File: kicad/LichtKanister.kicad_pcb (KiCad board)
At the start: 2 copper layers, 38 x 38 mm, 21 parts, among them J1 AVR-ISP-6, J2 Conn_01x04, J3 Conn_01x03, U1 ATmega48-20AU, U2 MAX485E, Y1 Crystal

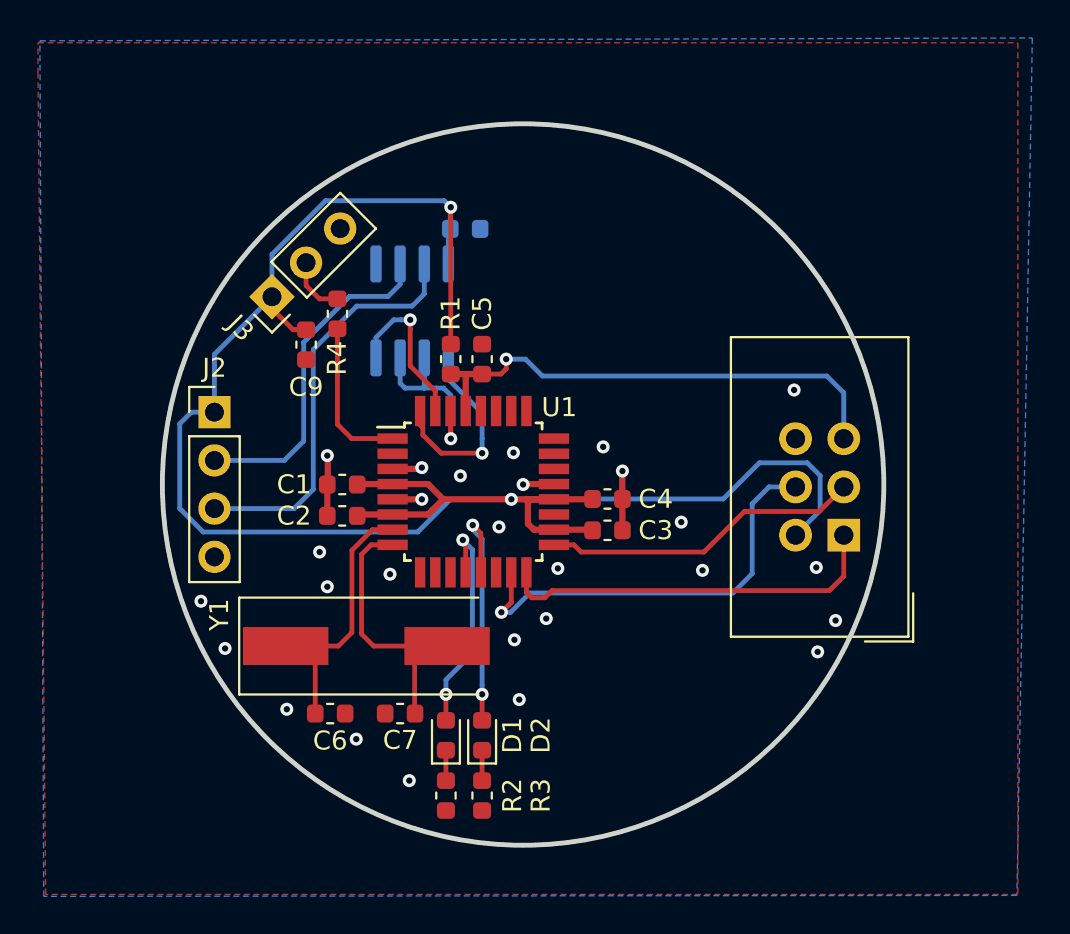
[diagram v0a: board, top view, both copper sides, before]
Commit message: added Mounting Holes, PinHeader for addressing first iteration of routing done
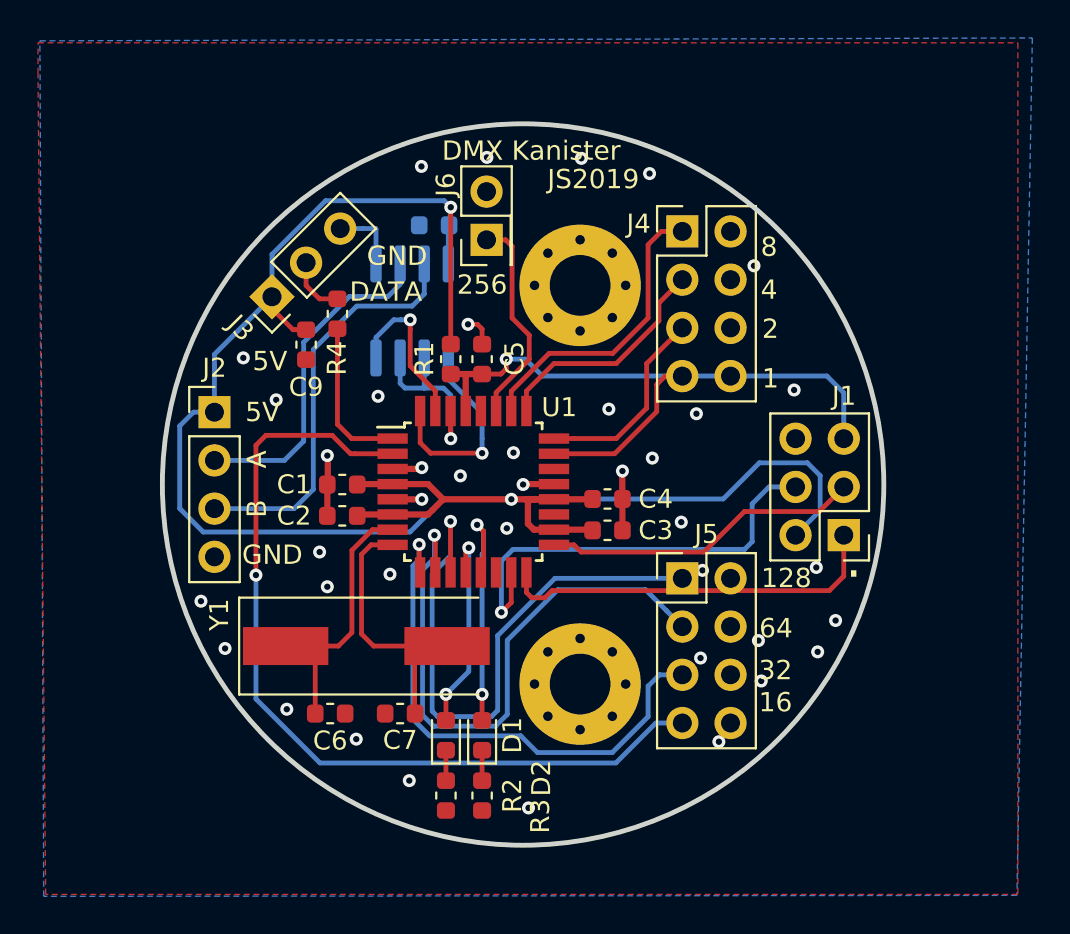
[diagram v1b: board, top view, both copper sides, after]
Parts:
- added H1: MountingHole_Pad, MountingHole:MountingHole_3.2mm_M3_Pad_Via, F.Cu at (73.5, 80.7)
- added H2: MountingHole_Pad, MountingHole:MountingHole_3.2mm_M3_Pad_Via, F.Cu at (73.5, 101.7)
- added J4: Conn_02x04_Odd_Even, Connector_PinHeader_2.54mm:PinHeader_2x04_P2.54mm_Vertical, F.Cu at (78.9, 77.9)
- added J5: Conn_02x04_Odd_Even, Connector_PinHeader_2.54mm:PinHeader_2x04_P2.54mm_Vertical, F.Cu at (78.9, 96.1)
- added J6: Conn_02x01, Connector_PinHeader_2.54mm:PinHeader_2x01_P2.54mm_Vertical, F.Cu at (68.6, 78.3)
- J1: footprint Connector_IDC:IDC-Header_2x03_P2.54mm_Vertical -> Connector_PinHeader_2.54mm:PinHeader_2x03_P2.54mm_Vertical
- moved C8 1.65 mm to (65.8, 77.5), turned to 180 degrees
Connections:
- U1 pad 10: Net-(U1-Pad10) -> /ADDR64
- U1 pad 11: Net-(U1-Pad11) -> /ADDR128
- U1 pad 2: Net-(U1-Pad2) -> /ADDR16
- U1 pad 23: Net-(U1-Pad23) -> /ADDR1
- U1 pad 24: Net-(U1-Pad24) -> /ADDR2
- U1 pad 25: Net-(U1-Pad25) -> /ADDR4
- U1 pad 26: Net-(U1-Pad26) -> /ADDR8
- U1 pad 27: Net-(U1-Pad27) -> /ADDR256
- U1 pad 9: Net-(U1-Pad9) -> /ADDR32
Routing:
- net /ADDR16: track 0.00 -> 45.9 mm, vias 0 -> 1
- net /ADDR64: track 0.00 -> 31.7 mm, vias 0 -> 1
- net /ADDR128: track 0.00 -> 31.7 mm, vias 0 -> 1
- net /ADDR32: track 0.00 -> 28.5 mm, vias 0 -> 1
- net /ADDR8: track 0.00 -> 15.8 mm
- net GND: track 11.1 -> 25.3 mm, vias 27 -> 39
- net /ADDR4: track 0.00 -> 12.2 mm
- net /ADDR256: track 0.00 -> 11.3 mm
- net /ADDR2: track 0.00 -> 10.5 mm
- net /ADDR1: track 0.00 -> 9.29 mm
- net Net-(D1-Pad2): track 12.1 -> 10.9 mm
- net /MOSI: track 22.7 -> 23.3 mm
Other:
- board text added: "."
- board text added: "1"
- board text added: "128"
- board text added: "16"
- board text added: "2"
- board text added: "256"
- board text added: "32"
- board text added: "4"
- board text added: "5V"
- board text added: "64"
- board text added: "8"
- board text added: "A"
- board text added: "B"
- board text added: "DATA"
- board text added: "DMX Kanister"
- board text added: "GND"
- board text added: "JS2019"

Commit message: fixed DRC violations
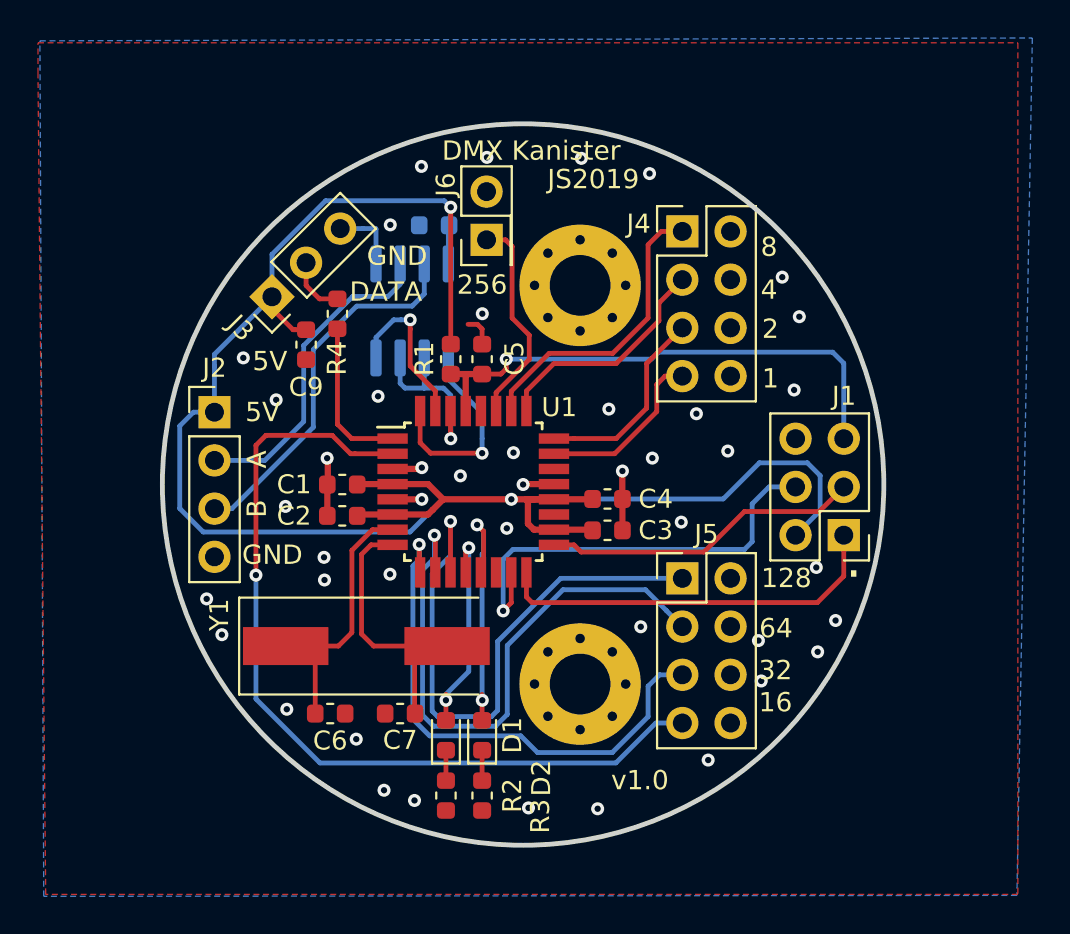
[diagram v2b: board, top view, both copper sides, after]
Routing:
- net /B: track 21.6 -> 19.7 mm
- net /RESET: track 26.3 -> 27.5 mm
- net /A: track 17.7 -> 17.0 mm
- net GND: vias 39 -> 44
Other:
- board text added: "v1.0"
